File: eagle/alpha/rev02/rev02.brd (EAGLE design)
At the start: 100 x 80 mm, 311 parts, among them CN1 HOST, IC3 N25Q128A13ES, Q3 2N7002, Q5 ASFL1, Q6 2N7002, T1 BC847, T2 BC847, T3 BC818, U1 LP3985IM5-3.3, U2 MC74HC1G14DTT1G, U3 ATTINY828R-AU, U4 MC14551BDG, U5 23K640-I/SN, U6 MCP79412-I/SN, U7 XC7A200TFBG484, Y1 12 MHz

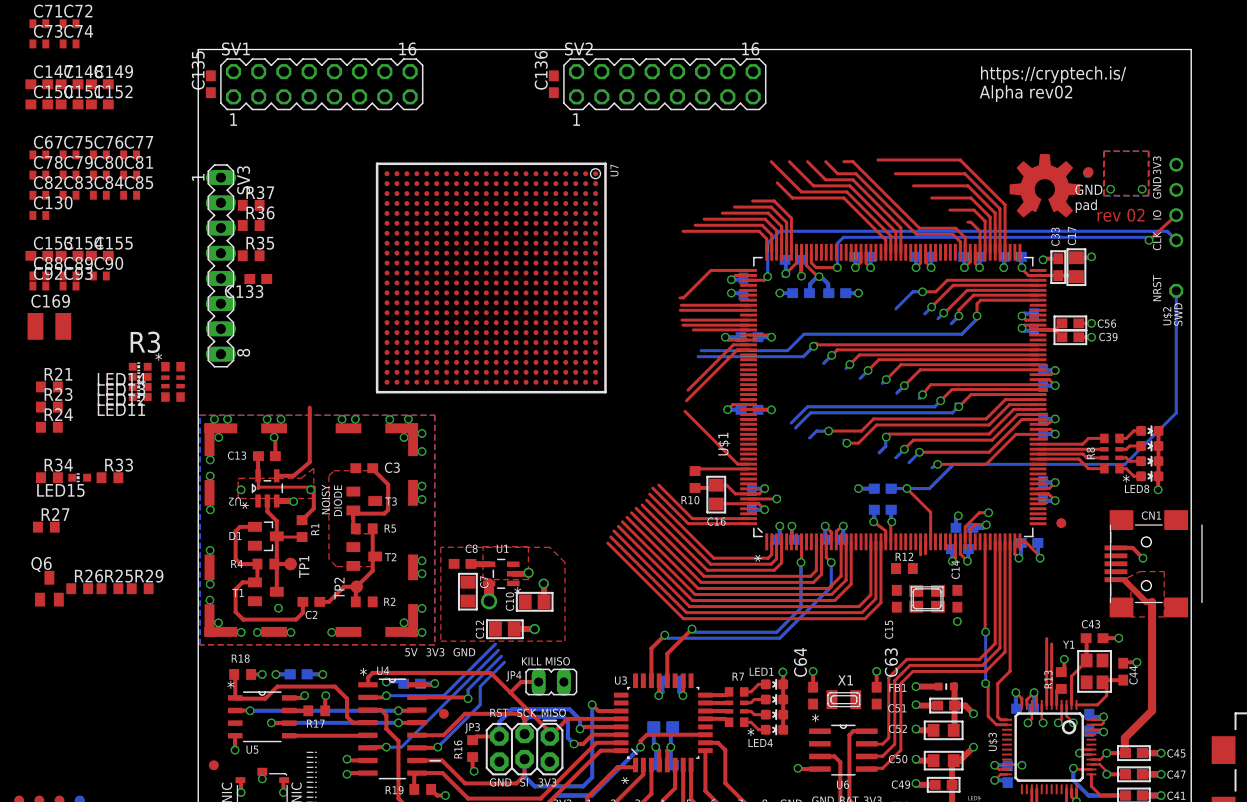
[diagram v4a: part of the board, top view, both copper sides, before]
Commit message: finished merging Pavel's FPGA schematics into the dev-bridge schematics.
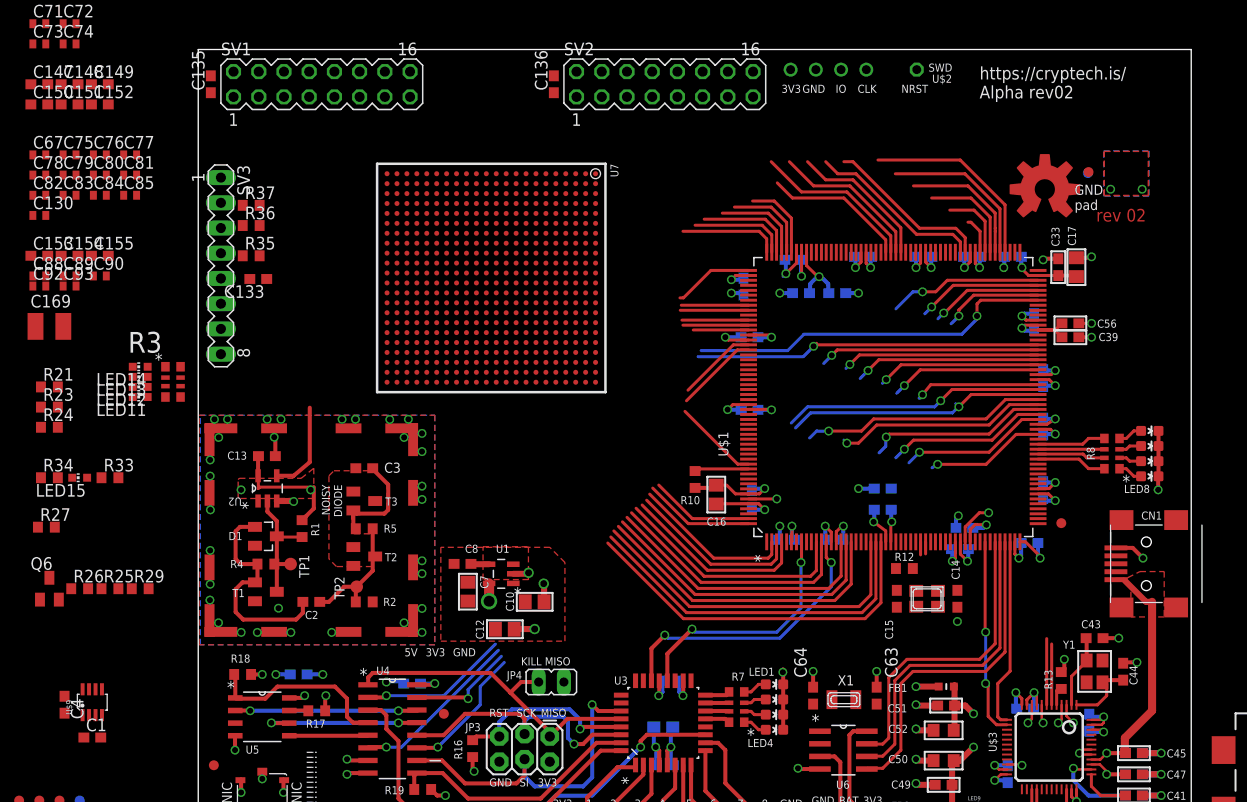
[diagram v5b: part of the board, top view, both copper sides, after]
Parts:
- added C1, C4: 10NF, rcl:C0603
- added U$9: LT3060, Alpha-Power:TSOT-8-23
- moved U$2 35.6 mm to (87.3, 78.7), turned to 270 degrees
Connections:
- removed net DIGITIZED: U2.4
- removed net FMC_CLK: U$1.167
- removed net FPGA_PROM_CS_B: U7.T19
- new net FPGA_ENTROPY_ENABLE: U$9.7
- new net IN: U$9.5, U$9.6
- new net N$1: C1.1, U$9.2
- new net N$2: C4.2, U$9.1
- net 15V_STABLE: now also C1.2, U$9.3, U$9.4
- net DIGITIZED_NOISE: now also U2.4
- net FPGA_FMC_CLK: now also U$1.167
- net FPGA_GPIO_TAMPER_0: now also U$1.183
- net FPGA_GPIO_TAMPER_1: now also U$1.182
- net FPGA_IRQ_N_0: now also U$1.181
- net FPGA_IRQ_N_1: now also U$1.180
- net FPGA_IRQ_N_2: now also U$1.179
- net FPGA_IRQ_N_3: now also U$1.178
- net FPGA_PROM_CS_N: now also U7.T19
- net GND: now also C4.1, U$9.8
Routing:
- net NRST: track 50.5 -> 0.00 mm, vias 1 -> 0
- net SWDCLK: track 47.5 -> 0.00 mm, vias 1 -> 0
- net SWDIO: track 42.4 -> 0.00 mm, vias 2 -> 0
- net DIGITIZED_NOISE: track 0.00 -> 9.32 mm
- net DIGITIZED: track 9.32 -> 0.00 mm
- net FPGA_FMC_CLK: track 0.00 -> 6.71 mm
- net FMC_CLK: track 6.71 -> 0.00 mm

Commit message: lots of updates after call with Pavel
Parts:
- removed C10: 1.0 uF, microbuilder:0805
- removed C12: 10 uF, microbuilder:0805
- removed C8: 10NF, rcl:C0603
- removed U1: LP3985IM5-3.3, LP3985IM5:SOT95P300X120-5N
- added C5: 2.2 uF LowESR, resistor:C0603
- added C6: 0.1uF, resistor:C0402
- added JP2: (no value), SparkFun-Connectors:1X03_LOCK
- added R22: 10K, resistor:R0402
- C1, C14, C15, C4: device rcl:C0603 -> rcl:C0402
- C16, C17: device microbuilder:0805 -> resistor:C0805
- C18, C19, C20, C21, C22, C23, C24, C25, C26, C27, C28, C29, C31, C32, C33, C34, C35, C36, C37, C40, C41, C42, C46, C48, C49, C51, C53, C54, C55: device microbuilder:0603 -> resistor:C0402
- C30, C38, C39, C45, C47, C56, C57: device microbuilder:0603 -> resistor:C0603
- C50, C52: device microbuilder:_0805 -> resistor:C0805
- C58: value 10 uF X7R 10v -> 10 uF; device microbuilder:0805 -> resistor:C0805
- C59, C60, C61, C62: value 0.1 uF X7R 10v -> 0.1 uF; device microbuilder:0603 -> resistor:C0402
- C7: value 1.0 uF -> 0.1 uF; device microbuilder:0805 -> resistor:C0402
- LED1, LED5: value B -> BLUE
- LED10, LED2, LED6: value G -> GREEN
- LED15, LED4, LED8: value R -> RED
- LED16: value (none) -> GREEN
- LED3, LED7, LED9: value Y -> YELLOW
- R10, R11, R12, R13, R14, R15, R16: device resistor:R0603 -> resistor:R0402
- U$9: value LT3060 -> LT3060ITS8-15
- moved C7 25.3 mm to (53.1, 1.52), turned to 0 degrees
- moved C1 2.84 mm to (10.7, 14.0)
- moved C4 2.84 mm to (7.87, 17.3)
- moved U$9 2.84 mm to (10.7, 17.5)
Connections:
- net !MKM_CS renamed MKM_CS_N
- net MKM_AVR_CS renamed MKM_AVR_CS_N
- net MKM_FPGA_CS renamed MKM_FPGA_CS_N
- removed net 3V3: C13.2, C16.1, C17.1, C18.1, C19.1, C20.1, C21.1, C22.1, C23.1, C24.1, C25.1, C26.1, C27.1, C28.1, C29.1, C30.1, C31.1, C32.1, C33.1, C34.1, C35.1, C36.1, C37.1, C38.1, C39.1, C56.1, C57.1, C7.1, JP6.1, R1.2, U$1.103, U$1.115, U$1.124, U$1.137, U$1.15, U$1.150, U$1.158, U$1.171, U$1.185, U$1.203, U$1.204, U$1.26, U$1.39, U$1.41, U$1.42, U$1.52, U$1.59, U$1.6, U$1.73, U$1.83, U$1.94, U$2.P$VCC, U1.5, U2.5, U6.8
- removed net FPGA_VCCO_3V3: C100.1, C101.1, C102.1, C105.1, C106.1, C107.1, C108.1, C109.1, C110.1, C113.1, C117.1, C118.1, C119.1, C120.1, C121.1, C122.1, C123.1, C124.1, C125.1, C126.1, C127.1, C128.1, C129.1, C133.1, C134.1, C135.1, C136.1, C156.1, C157.1, C158.1, C159.1, C160.1, C161.1, C162.1, C163.1, C164.1, C165.1, C166.1, C167.1, C170.1, C171.1, C172.1, C173.1, C97.1, C98.1, IC3.7, IC3.8, JP7.2, Q5.4, R25.2, R26.2, R27.2, R28.2, R33.2, R35.2, R36.2, R37.2, R49.2, R9.2, SV1.1, SV1.2, SV1.3, SV1.4, SV2.1, SV2.2, SV2.3, SV2.4, SV3.1, U7.A17, U7.AA17, U7.AA7, U7.AB14, U7.AB4, U7.B14, U7.C1, U7.C21, U7.D18, U7.E15, U7.F12, U7.F2, U7.F22, U7.G19, U7.H16, U7.H6, U7.J13, U7.J3, U7.K20, U7.L17, U7.M14, U7.M4, U7.N1, U7.N21, U7.P18, U7.R15, U7.R5, U7.T12, U7.T2, U7.T22, U7.U19, U7.U8, U7.V16, U7.V6, U7.W13, U7.W3, U7.Y10, U7.Y20
- removed net IN: U$9.5, U$9.6
- removed net N$8: C8.2, U1.4
- removed net VPGA_VCCO_3V3: R24.2
- new net 15V_LDO_ENABLE: JP2.2, R22.2, U$9.7
- new net FT_CTS: U$3.16
- new net FT_DTR: U$3.17
- new net FT_RTS: U$3.15
- new net VCC: C7.1, JP5.1
- new net VCCO_3V3: C100.1, C101.1, C102.1, C105.1, C106.1, C107.1, C108.1, C109.1, C110.1, C113.1, C117.1, C118.1, C119.1, C120.1, C121.1, C122.1, C123.1, C124.1, C125.1, C126.1, C127.1, C128.1, C129.1, C13.2, C133.1, C134.1, C135.1, C136.1, C156.1, C157.1, C158.1, C159.1, C16.1, C160.1, C161.1, C162.1, C163.1, C164.1, C165.1, C166.1, C167.1, C17.1, C170.1, C171.1, C172.1, C173.1, C18.1, C19.1, C20.1, C21.1, C22.1, C23.1, C24.1, C25.1, C26.1, C27.1, C28.1, C29.1, C30.1, C31.1, C32.1, C33.1, C34.1, C35.1, C36.1, C37.1, C38.1, C39.1, C56.1, C57.1, C6.1, C97.1, C98.1, IC3.7, IC3.8, JP6.1, JP7.2, Q5.4, R1.2, R24.2, R25.2, R26.2, R27.2, R28.2, R33.2, R35.2, R36.2, R37.2, R49.2, R9.2, SV1.1, SV1.2, SV1.3, SV1.4, SV2.1, SV2.2, SV2.3, SV2.4, SV3.1, U$1.103, U$1.115, U$1.124, U$1.137, U$1.15, U$1.150, U$1.158, U$1.171, U$1.185, U$1.203, U$1.204, U$1.26, U$1.39, U$1.41, U$1.42, U$1.52, U$1.59, U$1.6, U$1.73, U$1.83, U$1.94, U$2.P$VCC, U2.5, U6.8, U7.A17, U7.AA17, U7.AA7, U7.AB14, U7.AB4, U7.B14, U7.C1, U7.C21, U7.D18, U7.E15, U7.F12, U7.F2, U7.F22, U7.G19, U7.H16, U7.H6, U7.J13, U7.J3, U7.K20, U7.L17, U7.M14, U7.M4, U7.N1, U7.N21, U7.P18, U7.R15, U7.R5, U7.T12, U7.T2, U7.T22, U7.U19, U7.U8, U7.V16, U7.V6, U7.W13, U7.W3, U7.Y10, U7.Y20
- net 15V_STABLE: now also C5.1
- net 3V3_BATT: no longer JP5.1
- net FPGA_ENTROPY_ENABLE: now also JP2.1; no longer U$9.7
- net FPGA_GPIO_TAMPER_0: now also U3.25; no longer U$1.183
- net FPGA_GPIO_TAMPER_1: now also U3.26; no longer U$1.182
- net FPGA_INIT_B: now also U$1.176
- net FPGA_PROGRAM_B: now also U$1.177
- net GND: now also C5.2, C6.2; no longer C10.2, C12.2, C8.1, U1.2
- net PWR_18V: now also R22.1, U$9.5, U$9.6
- net VCC_5V0: no longer C10.1, C12.1, U1.1, U1.3
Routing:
- net 3V3: track 114.5 -> 0.00 mm, vias 28 -> 0
- net VCCO_3V3: track 0.00 -> 113.6 mm, vias 0 -> 27
- net GND: track 169.5 -> 159.7 mm, vias 64 -> 59
- net FT_VREGIN: track 26.6 -> 22.7 mm
- net N$8: track 1.84 -> 0.00 mm
- net FT_VPLL: track 17.0 -> 16.0 mm
- net FT_VPHY: track 21.0 -> 20.4 mm
- net 3V3_BATT: track 28.2 -> 28.8 mm
- net FT_VCC3V3: track 24.0 -> 24.6 mm
- added copper zone on layer 1, net VCCO_3V3
- added copper zone on layer 2, net VCCO_3V3
- removed copper zone on layer 1, net 3V3
- removed copper zone on layer 2, net 3V3
- removed copper zone on layer 1, net VCC_5V0

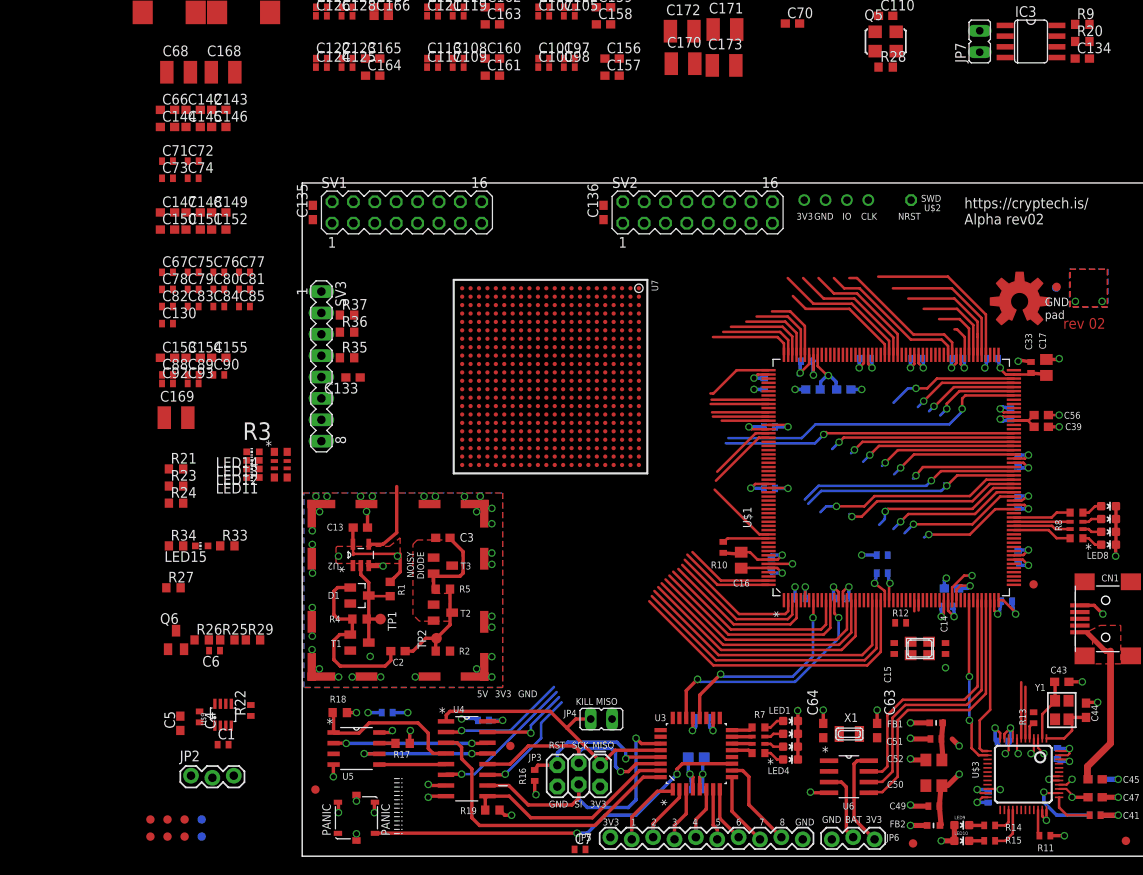
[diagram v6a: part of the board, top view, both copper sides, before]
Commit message: add more parts of the schematic (SRAM, analog switch for config mem)
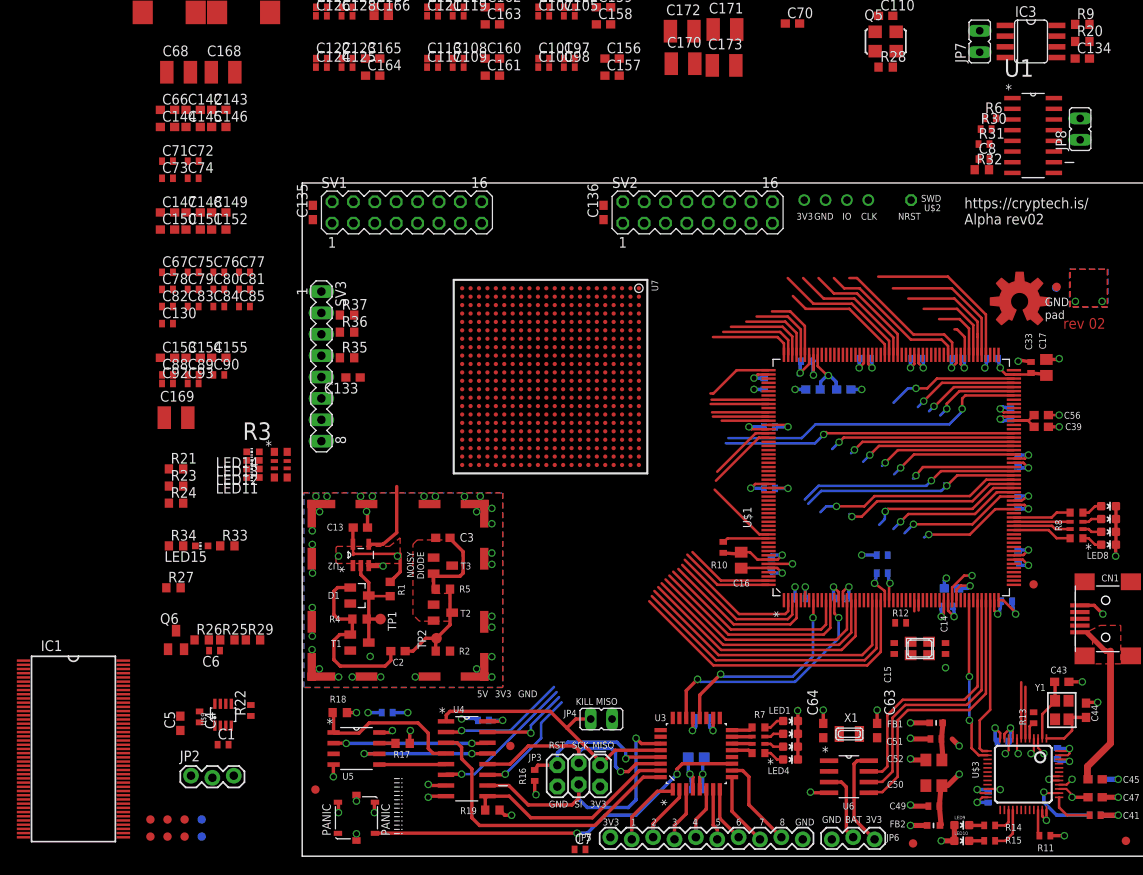
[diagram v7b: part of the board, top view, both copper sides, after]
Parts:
- added C8: 0.1 uF, resistor:C0402
- added IC1: IS45S32160F, Alpha-IC:TSOP2-86L
- added JP8: (no value), jumper:JP1
- added R30, R31, R6: 10K, resistor:R0402
- added R32: 15K, resistor:R0603
- added U1: MC14551BDG, ON_Semiconductor-MC14551BDG:SOIC127P600X175-16N
- LED11: value (none) -> BLUE
- LED12: value (none) -> GREEN
- LED13: value (none) -> YELLOW
- LED14: value (none) -> RED
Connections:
- new net ARM_FPGA_CFG_CONTROL: JP8.2, U$1.166
- new net ARM_FPGA_CFG_CS_N: U1.3
- new net ARM_FPGA_CFG_MISO: U$1.162, U1.1
- new net ARM_FPGA_CFG_MOSI: U$1.163, U1.10
- new net ARM_FPGA_CFG_SCLK: U$1.161, U1.12
- new net FPGA_CFG_CS_N: U1.4, U7.T19
- new net FPGA_CFG_MISO: U1.14, U7.R22
- new net FPGA_CFG_MOSI: U1.5, U7.P22
- new net FPGA_CFG_SCLK: U1.13, U7.L12
- new net N$3: JP8.1, R32.2, U1.9
- new net VDD: IC1.1, IC1.15, IC1.29, IC1.43
- new net VDDQ: IC1.3, IC1.35, IC1.41, IC1.49, IC1.55, IC1.75, IC1.81
- new net VSS: IC1.44, IC1.58, IC1.72, IC1.86
- new net VSSQ: IC1.12, IC1.32, IC1.38, IC1.46, IC1.52, IC1.6, IC1.78, IC1.84
- net 3V3_BATT: now also C8.1, U1.16
- net FMC_D0: now also IC1.2
- net FMC_D1: now also IC1.4
- net FMC_D10: now also IC1.77
- net FMC_D11: now also IC1.79
- net FMC_D12: now also IC1.80
- net FMC_D13: now also IC1.82
- net FMC_D14: now also IC1.83
- net FMC_D15: now also IC1.85
- net FMC_D16: now also IC1.31
- net FMC_D17: now also IC1.33
- net FMC_D18: now also IC1.34, IC1.36
- net FMC_D2: now also IC1.5
- net FMC_D20: now also IC1.37
- net FMC_D21: now also IC1.39
- net FMC_D22: now also IC1.40
- net FMC_D23: now also IC1.42
- net FMC_D24: now also IC1.45
- net FMC_D25: now also IC1.47
- net FMC_D26: now also IC1.48
- net FMC_D27: now also IC1.50
- net FMC_D28: now also IC1.51
- net FMC_D29: now also IC1.53
- net FMC_D3: now also IC1.7
- net FMC_D30: now also IC1.54
- net FMC_D31: now also IC1.56
- net FMC_D4: now also IC1.8
- net FMC_D5: now also IC1.10
- net FMC_D6: now also IC1.11
- net FMC_D7: now also IC1.13
- net FMC_D8: now also IC1.74
- net FMC_D9: now also IC1.76
- net FPGA_PROM_CS_N: now also U1.2; no longer U7.T19
- net FPGA_PROM_MISO: now also U1.15; no longer U7.R22
- net FPGA_PROM_MOSI: now also U1.6; no longer U7.P22
- net FPGA_PROM_SCLK: now also U1.11; no longer U7.L12
- net GND: now also C8.2, R32.1, U1.7, U1.8
- net RTC_MFP: now also R6.2
- net RTC_SCL: now also R30.2
- net RTC_SDA: now also R31.2
- net VCC: now also R30.1, R31.1, R6.1
